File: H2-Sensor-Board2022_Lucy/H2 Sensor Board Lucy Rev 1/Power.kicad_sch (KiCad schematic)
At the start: 41 parts, among them J2 Conn_02x03_Top_Bottom, Q1 NMOS, U3 AZ1117H-5.0, U4 TPS2596, U6 AZ1117EH-3.3

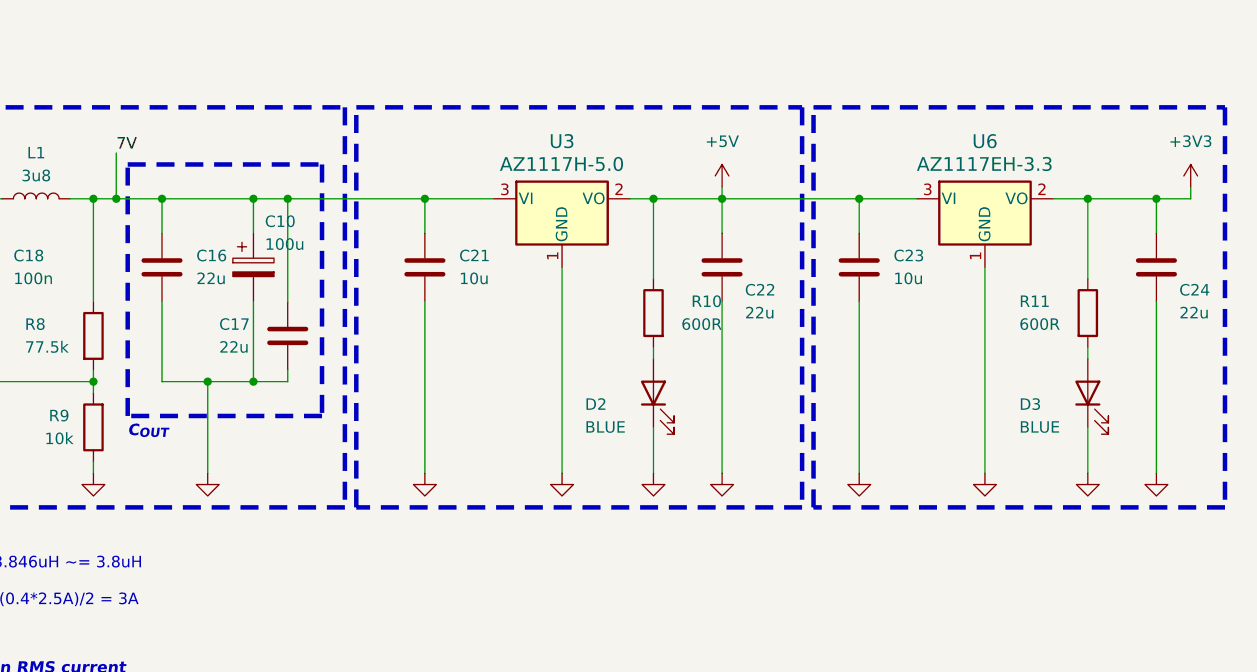
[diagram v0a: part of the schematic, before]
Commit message: Changed Bulk caps and added them to LDO out instead of buck
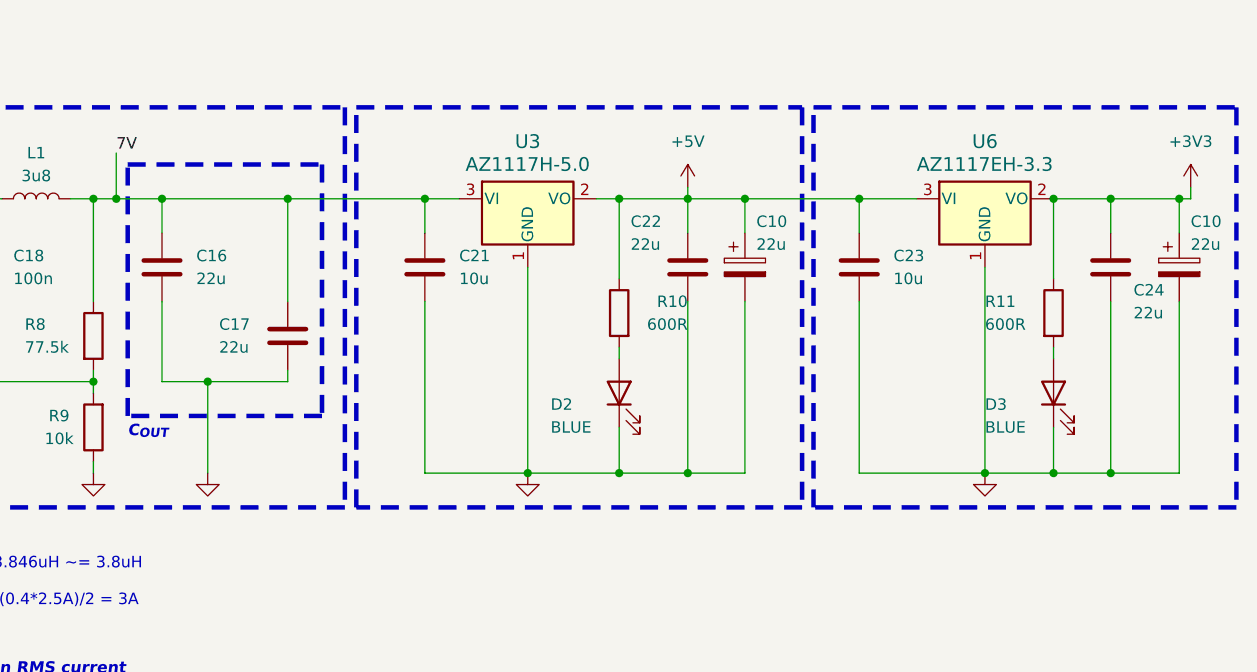
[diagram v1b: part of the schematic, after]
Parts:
- added C10: 22u, Capacitor_SMD:CP_Elec_6.3x5.9, symbol Device:C_Polarized
- C10: value 100u -> 22u; DK # 399-A766EB127M0JLAE022CT-ND -> 732-13321-1-ND
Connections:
- net +3V3: now also C10.1
- net +5V: now also C10.1
- net 7V: no longer C10.1
- net GND: now also C10.2
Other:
- moved on the sheet: C10, C22, C24, D2, D3, R10, R11, U3

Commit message: Finished
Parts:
- R10: value 600R -> 500R
- R11: value 600R -> 160R
- R4: value 47k -> 47k5
- R5: value 13k -> 30k1
- R6: value 450k -> 442k
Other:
- note added: "From data sheet V_{OVLO} = 1.2V V_{UVLO} = 1.2V 1. V_{IN(ON)} = V_{OVLO(R} * (R1 + R2)/R2 2. V_{UVLO} = r2 + r3/ (r1 + r2 + r3) * V_{IN(UV)} 3. V_{OVLO} = r3 / (r1 + r2 + r3) * V_{IN(OV)} V_{OV} = 13V V_{UV} = 8V 1% r1 = 442k, r2 = 30k1, r3 = 47k5 V_{approx, OV} = 13.1267V V_{approx, UV} = 8.035} rilm max = 464R; will give max 1.94A 845R will give 1A"
- note removed: "From data sheet V_{OVLO} = 1.2V V_{UVLO} = 1.2V 1. V_{IN(ON)} = V_{OVLO(R} * (R1 + R2)/R2 2. V_{UVLO} = r2 + r3/ (r1 + r2 + r3) * V_{IN(UV)} 3. V_{OVLO} = r3 / (r1 + r2 + r3) * V_{IN(OV)} V_{OV} = 13V V_{UV} = 10V r3 = 1M; r2 = 31.5k = 32k; r3 = 104.9k = 105k rilm max = 464R; will give max 1.94A 845R will give 1A"
- moved on the sheet: D1, J2, Q1, R7

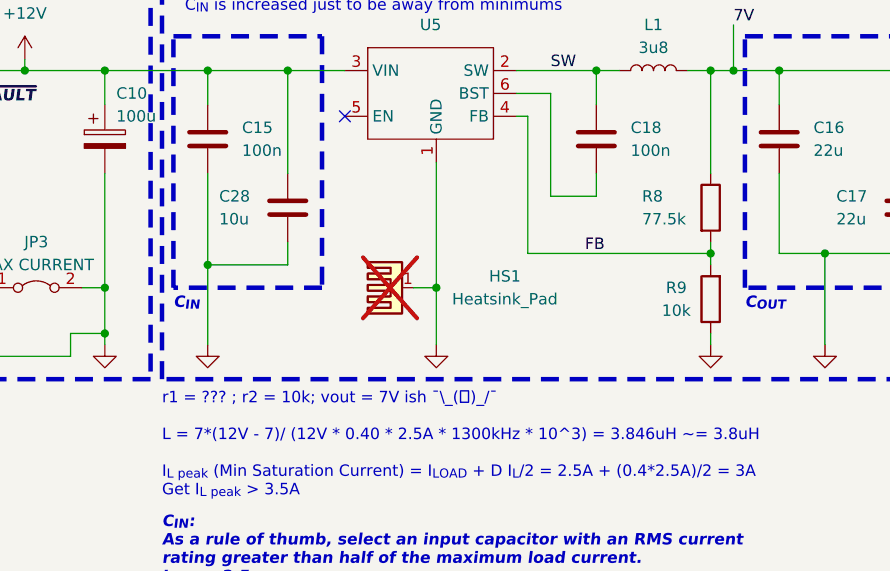
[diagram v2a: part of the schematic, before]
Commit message: added inrush current limiting cap and changed buck out voltage selection voltage divider resistors to standard values
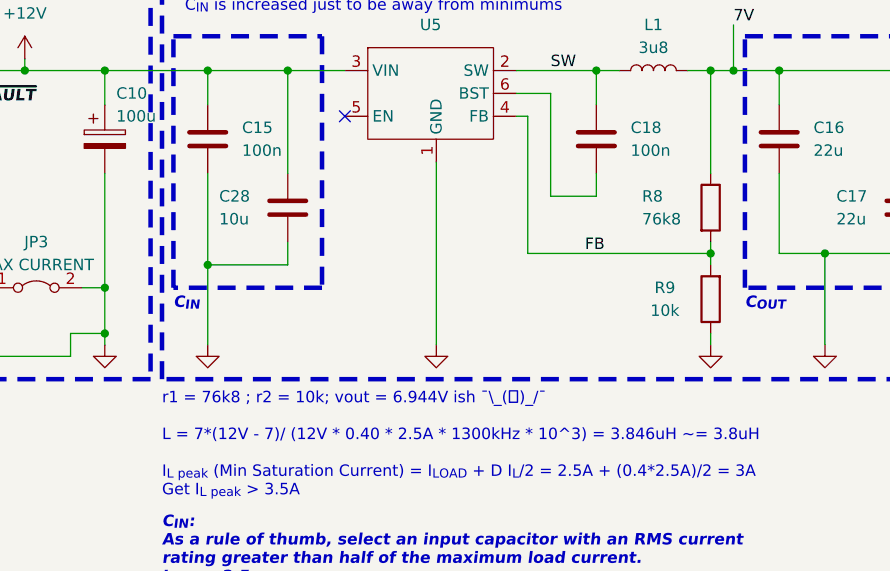
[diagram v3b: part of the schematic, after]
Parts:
- removed HS1: Heatsink_Pad, Heatsink:Heatsink_35x26mm_1xFixation3mm_Fischer-SK486-35, symbol Mechanical:Heatsink_Pad
- R8: value 77.5k -> 76k8
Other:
- note added: "r1 = 76k8 ; r2 = 10k; vout = 6.944V ish ¯\_(ツ)_/¯ L = 7*(12V - 7)/ (12V * 0.40 * 2.5A * 1300kHz * 10^3) = 3.846uH ~= 3.8uH I_{L peak} (Min Saturation Current) = I_{LOAD} + D I_{L}/2 = 2.5A + (0.4*2.5A)/2 = 3A Get I_{L peak} > 3.5A"
- note removed: "r1 = ??? ; r2 = 10k; vout = 7V ish ¯\_(ツ)_/¯ L = 7*(12V - 7)/ (12V * 0.40 * 2.5A * 1300kHz * 10^3) = 3.846uH ~= 3.8uH I_{L peak} (Min Saturation Current) = I_{LOAD} + D I_{L}/2 = 2.5A + (0.4*2.5A)/2 = 3A Get I_{L peak} > 3.5A"
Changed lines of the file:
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@@
   (junction (at 154.94 60.96) (diameter 0) (color 0 0 0 0)
-  )
-  (junction (at 124.46 64.77) (diameter 0) (color 0 0 0 0)
   )
   (junction (at 58.42 55.88) (diameter 0) (color 0 0 0 0)
@@
     (stroke (width 0) (type default))
   )
-  (wire (pts (xy 124.46 50.8) (xy 124.46 64.77))
-    (stroke (width 0) (type default))
-  )
   (wire (pts (xy 99.06 40.64) (xy 107.95 40.64))
     (stroke (width 0) (type default))
@@
     (stroke (width 0) (type default))
   )
-  (wire (pts (xy 121.92 64.77) (xy 124.46 64.77))
-    (stroke (width 0) (type default))
-  )
   (wire (pts (xy 40.64 60.96) (xy 45.72 60.96))
     (stroke (width 0) (type default))
@@
     (stroke (width 0) (type default))
   )
-  (wire (pts (xy 124.46 64.77) (xy 124.46 71.12))
+  (wire (pts (xy 124.46 50.8) (xy 124.46 71.12))
     (stroke (width 0) (type default))
   )
@@
     (effects (font (size 1.27 1.27) (thickness 0.254) bold) (justify left bottom))
   )
-  (text "r1 = ??? ; r2 = 10k; vout = 7V ish ¯\\_(ツ)_/¯\n\nL = 7*(12V - 7)/ (12V * 0.40 * 2.5A * 1300kHz * 10^3) = 3.846uH ~= 3.8uH\n\nI_{L peak} (Min Saturation Current) = I_{LOAD} + D I_{L}/2 = 2.5A + (0.4*2.5A)/2 = 3A\nGet I_{L peak} > 3.5A\n\n"
+  (text "r1 = 76k8 ; r2 = 10k; vout = 6.944V ish ¯\\_(ツ)_/¯\n\nL = 7*(12V - 7)/ (12V * 0.40 * 2.5A * 1300kHz * 10^3) = 3.846uH ~= 3.8uH\n\nI_{L peak} (Min Saturation Current) = I_{LOAD} + D I_{L}/2 = 2.5A + (0.4*2.5A)/2 = 3A\nGet I_{L peak} > 3.5A\n\n"
     (at 93.98 90.17 0)
     (effects (font (size 1.27 1.27)) (justify left bottom))
@@
     )
   )
-  (symbol (lib_id "Mechanical:Heatsink_Pad") (at 119.38 64.77 90) (unit 1)
-    (in_bom no) (on_board no) (dnp yes)
-    (property "Reference" "HS1" (at 132.08 63.5 90)
-      (effects (font (size 1.27 1.27)))
-    )
-    (property "Value" "Heatsink_Pad" (at 132.08 66.04 90)
-      (effects (font (size 1.27 1.27)))
-    )
-    (property "Footprint" "Heatsink:Heatsink_35x26mm_1xFixation3mm_Fischer-SK486-35" (at 120.65 64.4652 0)
-      (effects (font (size 1.27 1.27)) hide)
-    )
-    (property "Datasheet" "~" (at 120.65 64.4652 0)
-      (effects (font (size 1.27 1.27)) hide)
-    )
-    (pin "1")
-    (instances
-      (project "H2 Sensor Board Lucy Rev 1"
-        (path "/61fdd4a1-2d1e-44dc-8644-252e12d35745/3bc5ea2f-35c7-4100-bf1f-fa9268f700b9"
-          (reference "HS1") (unit 1)
-        )
-      )
-    )
-  )
   (symbol (lib_id "Connector_Generic:Conn_02x03_Top_Bottom") (at 43.18 130.81 0) (unit 1)
     (in_bom yes) (on_board yes) (dnp no) (fields_autoplaced)
@@
       (effects (font (size 1.27 1.27)) (justify left))
     )
-    (property "Value" "77.5k" (at 147.32 57.15 0)
+    (property "Value" "76k8" (at 147.32 57.15 0)
       (effects (font (size 1.27 1.27)) (justify left))
     )
@@
   (symbol (lib_id "Device:R") (at 154.94 66.04 180) (unit 1)
     (in_bom yes) (on_board yes) (dnp no)
-    (property "Reference" "R9" (at 151.13 64.77 0)
-      (effects (font (size 1.27 1.27)))
-    )
-    (property "Value" "10k" (at 151.13 67.31 0)
-      (effects (font (size 1.27 1.27)))
-    )
+    (property "Reference" "R9" (at 149.86 64.77 0)
+      (effects (font (size 1.27 1.27)))
+    )
+    (property "Value" "10k" (at 149.86 67.31 0)
+      (effects (font (size 1.27 1.27)))
+    )

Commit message: shit forgot to save
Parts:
- added C32: 2n2, Capacitor_SMD:C_0402_1005Metric, symbol Device:C
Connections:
- net GND: now also C32.2
- net at U4.2 (dV/dT): now also C32.1
- no-connect marks 4 -> 3
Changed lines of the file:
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@@
   (junction (at 167.64 60.96) (diameter 0) (color 0 0 0 0)
+  )
+  (junction (at 58.42 68.58) (diameter 0) (color 0 0 0 0)
   )
   (junction (at 162.56 40.64) (diameter 0) (color 0 0 0 0)
@@
   (no_connect (at 63.5 133.35))
   (no_connect (at 25.4 133.35))
-  (no_connect (at 55.88 54.61))
   (no_connect (at 114.3 45.72))
   (wire (pts (xy 167.64 60.96) (xy 167.64 71.12))
@@
     (stroke (width 0) (type default))
   )
+  (wire (pts (xy 52.07 57.15) (xy 52.07 55.88))
+    (stroke (width 0) (type default))
+  )
   (wire (pts (xy 40.64 60.96) (xy 40.64 59.69))
     (stroke (width 0) (type default))
@@
     (stroke (width 0) (type default))
   )
+  (wire (pts (xy 52.07 55.88) (xy 55.88 55.88))
+    (stroke (width 0) (type default))
+  )
   (wire (pts (xy 254 71.12) (xy 261.62 71.12))
     (stroke (width 0) (type default))
@@
     (stroke (width 0) (type default))
   )
-  (wire (pts (xy 58.42 55.88) (xy 58.42 71.12))
+  (wire (pts (xy 58.42 55.88) (xy 58.42 68.58))
     (stroke (width 0) (type default))
   )
@@
     (stroke (width 0) (type default))
   )
+  (wire (pts (xy 58.42 68.58) (xy 58.42 71.12))
+    (stroke (width 0) (type default))
+  )
   (wire (pts (xy 275.59 40.64) (xy 275.59 44.45))
     (stroke (width 0) (type default))
@@
     (stroke (width 0) (type default))
   )
+  (wire (pts (xy 52.07 64.77) (xy 52.07 68.58))
+    (stroke (width 0) (type default))
+  )
   (wire (pts (xy 105.41 148.59) (xy 107.95 148.59))
     (stroke (width 0) (type default))
@@
     (stroke (width 0) (type default))
   )
+  (wire (pts (xy 52.07 68.58) (xy 58.42 68.58))
+    (stroke (width 0) (type default))
+  )
   (wire (pts (xy 134.62 60.96) (xy 154.94 60.96))
     (stroke (width 0) (type default))
@@
   )
   (wire (pts (xy 58.42 55.88) (xy 58.42 54.61))
+    (stroke (width 0) (type default))
+  )
+  (wire (pts (xy 55.88 55.88) (xy 55.88 54.61))
     (stroke (width 0) (type default))
   )
@@
         )
       )
+    )
+  )
+  (symbol (lib_id "Device:C") (at 52.07 60.96 0) (unit 1)
+    (in_bom yes) (on_board yes) (dnp no)
+    (property "Reference" "C32" (at 45.72 64.77 0)
+      (effects (font (size 1.27 1.27)) (justify left))
+    )
+    (property "Value" "2n2" (at 45.72 67.31 0)
+      (effects (font (size 1.27 1.27)) (justify left))
+    )
+    (property "Footprint" "Capacitor_SMD:C_0402_1005Metric" (at 53.0352 64.77 0)
+      (effects (font (size 1.27 1.27)) hide)
+    )
+    (property "Datasheet" "~" (at 52.07 60.96 0)
+      (effects (font (size 1.27 1.27)) hide)
+    )
+    (pin "1")
+    (pin "2")
+    (instances
+      (project "H2 Sensor Board Lucy Rev 1"
+        (path "/61fdd4a1-2d1e-44dc-8644-252e12d35745/3bc5ea2f-35c7-4100-bf1f-fa9268f700b9"
+          (reference "C32") (unit 1)
+        )
+      )

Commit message: fixzed some stuffs
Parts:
- added R27: 34k, Resistor_SMD:R_0603_1608Metric, symbol Device:R
- added R28: 47k5, Resistor_SMD:R_0603_1608Metric, symbol Device:R
- R3: footprint Resistor_SMD:R_0805_2012Metric -> Resistor_SMD:R_0603_1608Metric
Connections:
- net 12V_UP: now also R28.1; no longer R3.2
- net GND: now also R27.1
- new net: R27.2, R28.2, R3.2
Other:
- moved on the sheet: D1, Q1, R3, R7

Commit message: Fixed some stuffs
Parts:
- C15, C18: JLCPCB Part#(Optional) (none) -> C1525
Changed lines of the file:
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@@
+      (effects (font (size 1.27 1.27)) hide)
+    )
+    (property "JLCPCB Part#(Optional)" "C1525" (at 142.24 48.26 0)
       (effects (font (size 1.27 1.27)) hide)
     )
@@
       (effects (font (size 1.27 1.27)) hide)
     )
+    (property "JLCPCB Part#(Optional)" "C1525" (at 99.06 48.26 0)
+      (effects (font (size 1.27 1.27)) hide)
+    )
